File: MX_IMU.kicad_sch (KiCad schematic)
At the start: 31 parts, among them SW1 SW_SPST, U1 ld39150dt33-r, U200 STM32F405RGT6, U4 AT24C256, Y200 16MHz

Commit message: update
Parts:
- removed C4: 2u2, Capacitor_SMD:C_0603_1608Metric, symbol Device:C
- added C5: 2u2, Capacitor_SMD:C_0603_1608Metric, symbol Device:C_Small
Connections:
- net +3.3V: now also C5.1
- net GND: now also C5.2
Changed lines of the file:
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@@
 	(wire
 		(pts
-			(xy 203.2 35.56) (xy 203.2 34.29)
+			(xy 203.2 31.75) (xy 203.2 35.56)
 		)
 		(stroke
@@
 	(symbol
 		(lib_id "Device:C")
-		(at 203.2 30.48 0)
+		(at 177.8 30.48 0)
 		(unit 1)
 		(exclude_from_sim no)
@@
 		(on_board yes)
 		(dnp no)
-		(property "Reference" "C4"
-			(at 205.74 29.21 0)
+		(property "Reference" "C3"
+			(at 180.34 29.21 0)
 			(effects
 				(font
@@
 			)
 		)
-		(property "Value" "2u2"
-			(at 205.74 31.75 0)
+		(property "Value" "1u"
+			(at 180.34 31.75 0)
 			(effects
 				(font
@@
 		)
 		(property "Footprint" "Capacitor_SMD:C_0603_1608Metric"
-			(at 204.1652 34.29 0)
+			(at 178.7652 34.29 0)
 			(effects
 				(font
@@
 		)
 		(property "Datasheet" "~"
-			(at 203.2 30.48 0)
+			(at 177.8 30.48 0)
 			(effects
 				(font
@@
 		)
 		(property "Description" "Unpolarized capacitor"
-			(at 203.2 30.48 0)
+			(at 177.8 30.48 0)
 			(effects
 				(font
@@
 			(project "MX_IMU"
 				(path "/8ed38441-7d4e-4e89-870f-07e11c6dce38"
-					(reference "C4")
+					(reference "C3")
 					(unit 1)
 				)
@@
 	)
 	(symbol
-		(lib_id "Device:C")
-		(at 177.8 30.48 0)
+		(lib_id "Device:R_Small_US")
+		(at 241.3 80.01 0)
 		(unit 1)
 		(exclude_from_sim no)
@@
 		(on_board yes)
 		(dnp no)
-		(property "Reference" "C3"
-			(at 180.34 29.21 0)
+		(fields_autoplaced yes)
+		(property "Reference" "R14"
+			(at 243.078 78.7399 0)
 			(effects
 				(font
@@
 			)
 		)
-		(property "Value" "1u"
-			(at 180.34 31.75 0)
+		(property "Value" "330R"
+			(at 243.078 81.2799 0)
 			(effects
 				(font
@@
 			)
 		)
-		(property "Footprint" "Capacitor_SMD:C_0603_1608Metric"
-			(at 178.7652 34.29 0)
+		(property "Footprint" "Resistor_SMD:R_0402_1005Metric"
+			(at 241.3 80.01 0)
 			(effects
 				(font
@@
 		)
 		(property "Datasheet" "~"
-			(at 177.8 30.48 0)
+			(at 241.3 80.01 0)
 			(effects
 				(font
@@
 			)
 		)
-		(property "Description" "Unpolarized capacitor"
-			(at 177.8 30.48 0)
+		(property "Description" ""
+			(at 241.3 80.01 0)
 			(effects
 				(font
@@
 			(project "MX_IMU"
 				(path "/8ed38441-7d4e-4e89-870f-07e11c6dce38"
-					(reference "C3")
+					(reference "R14")
 					(unit 1)
 				)
@@
 	)
 	(symbol
-		(lib_id "Device:R_Small_US")
-		(at 241.3 80.01 0)
+		(lib_id "power:GND")
+		(at 241.3 96.52 0)
 		(unit 1)
 		(exclude_from_sim no)
@@
 		(dnp no)
 		(fields_autoplaced yes)
-		(property "Reference" "R14"
-			(at 243.078 78.7399 0)
+		(property "Reference" "#PWR038"
+			(at 241.3 102.87 0)
 			(effects
 				(font
 					(size 1.27 1.27)
 				)
-				(justify left)
+				(hide yes)
 			)
 		)
-		(property "Value" "330R"
-			(at 243.078 81.2799 0)
+		(property "Value" "GND"
+			(at 241.3 101.6 0)
 			(effects
 				(font
 					(size 1.27 1.27)
 				)
-				(justify left)
+				(hide yes)
 			)
 		)
-		(property "Footprint" "Resistor_SMD:R_0402_1005Metric"
-			(at 241.3 80.01 0)
+		(property "Footprint" ""
+			(at 241.3 96.52 0)
 			(effects
 				(font
@@
 			)
 		)
-		(property "Datasheet" "~"
-			(at 241.3 80.01 0)
+		(property "Datasheet" ""
+			(at 241.3 96.52 0)
 			(effects
 				(font
@@
 		)
 		(property "Description" ""
-			(at 241.3 80.01 0)
+			(at 241.3 96.52 0)
 			(effects
 				(font
 					(size 1.27 1.27)
 				)
-				(hide yes)
 			)
 		)
 		(pin "1"
 		)
-		(pin "2"
-		)
 		(instances
 			(project "MX_IMU"
 				(path "/8ed38441-7d4e-4e89-870f-07e11c6dce38"
-					(reference "R14")
+					(reference "#PWR038")
 					(unit 1)
 				)
@@
 	)
 	(symbol
-		(lib_id "power:GND")
-		(at 241.3 96.52 0)
+		(lib_id "Device:C_Small")
+		(at 203.2 29.21 0)
 		(unit 1)
 		(exclude_from_sim no)
@@
 		(on_board yes)
 		(dnp no)
-		(fields_autoplaced yes)
-		(property "Reference" "#PWR038"
-			(at 241.3 102.87 0)
+		(property "Reference" "C5"
+			(at 205.74 27.94 0)
 			(effects
 				(font
 					(size 1.27 1.27)
 				)
-				(hide yes)
+				(justify left)
 			)
 		)
-		(property "Value" "GND"
-			(at 241.3 101.6 0)
+		(property "Value" "2u2"
+			(at 205.74 30.48 0)
 			(effects
 				(font
 					(size 1.27 1.27)
 				)
-				(hide yes)
+				(justify left)
 			)
 		)
-		(property "Footprint" ""
-			(at 241.3 96.52 0)
+		(property "Footprint" "Capacitor_SMD:C_0603_1608Metric"
+			(at 203.2 29.21 0)
 			(effects
 				(font
@@
 			)
 		)
-		(property "Datasheet" ""
-			(at 241.3 96.52 0)
+		(property "Datasheet" "~"
+			(at 203.2 29.21 0)
 			(effects
 				(font
@@
 		)
 		(property "Description" ""
-			(at 241.3 96.52 0)
+			(at 203.2 29.21 0)
+			(effects
+				(font
+					(size 1.27 1.27)
+				)
+			)
+		)
+		(property "LCSC Part #" "C23630"
+			(at 203.2 29.21 0)
 			(effects
 				(font
 					(size 1.27 1.27)
 				)
+				(hide yes)
 			)
 		)
 		(pin "1"
 		)
+		(pin "2"
+		)
 		(instances
 			(project "MX_IMU"
 				(path "/8ed38441-7d4e-4e89-870f-07e11c6dce38"
-					(reference "#PWR038")
+					(reference "C5")
 					(unit 1)
 				)

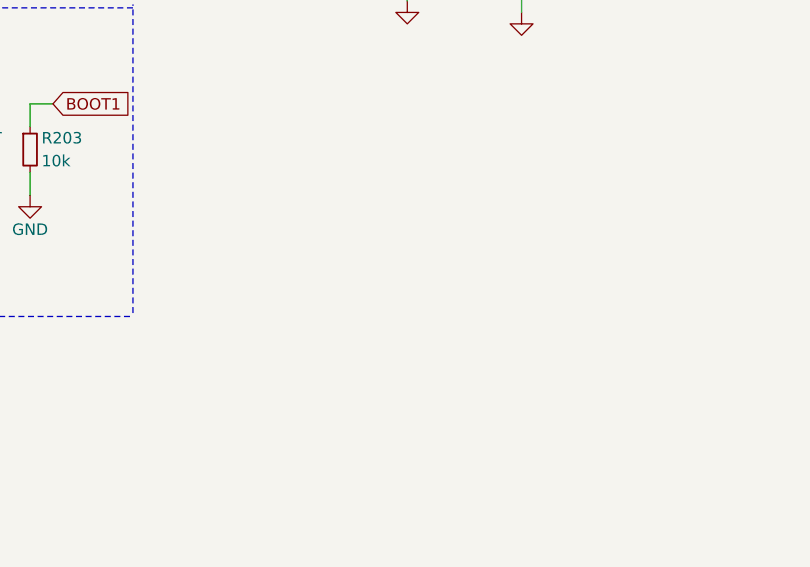
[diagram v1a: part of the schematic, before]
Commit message: add mountinghole in sch
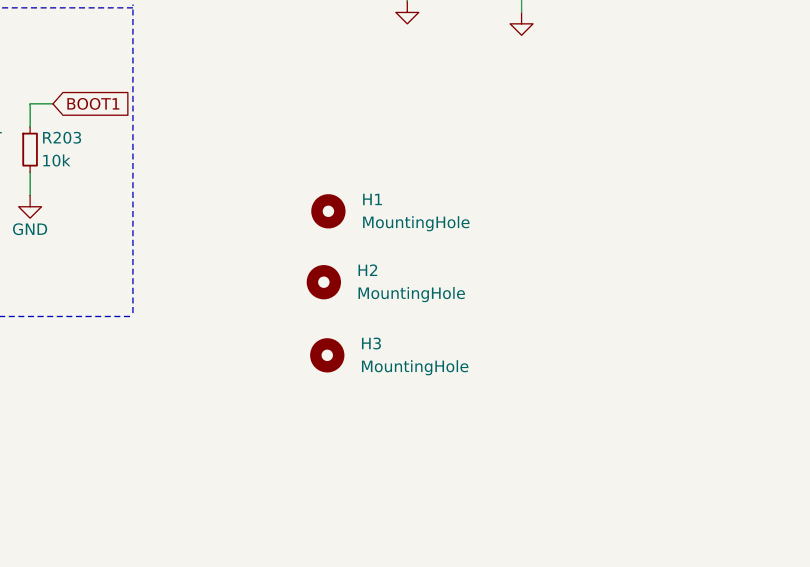
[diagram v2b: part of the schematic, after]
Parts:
- added H1, H2, H3: MountingHole, MountingHole:MountingHole_2mm, symbol Mechanical:MountingHole
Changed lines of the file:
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@@
+	)
+	(symbol
+		(lib_id "Mechanical:MountingHole")
+		(at 219.71 134.62 0)
+		(unit 1)
+		(exclude_from_sim no)
+		(in_bom no)
+		(on_board yes)
+		(dnp no)
+		(fields_autoplaced yes)
+		(property "Reference" "H3"
+			(at 223.393 133.3499 0)
+			(effects
+				(font
+					(size 1.27 1.27)
+				)
+				(justify left)
+			)
+		)
+		(property "Value" "MountingHole"
+			(at 223.393 135.8899 0)
+			(effects
+				(font
+					(size 1.27 1.27)
+				)
+				(justify left)
+			)
+		)
+		(property "Footprint" "MountingHole:MountingHole_2mm"
+			(at 219.71 134.62 0)
+			(effects
+				(font
+					(size 1.27 1.27)
+				)
+				(hide yes)
+			)
+		)
+		(property "Datasheet" "~"
+			(at 219.71 134.62 0)
+			(effects
+				(font
+					(size 1.27 1.27)
+				)
+				(hide yes)
+			)
+		)
+		(property "Description" "Mounting Hole without connection"
+			(at 219.71 134.62 0)
+			(effects
+				(font
+					(size 1.27 1.27)
+				)
+				(hide yes)
+			)
+		)
+		(instances
+			(project "MX_IMU"
+				(path "/8ed38441-7d4e-4e89-870f-07e11c6dce38"
+					(reference "H3")
+					(unit 1)
+				)
+			)
+		)
 	)
 	(symbol
@@
 	)
 	(symbol
+		(lib_id "Mechanical:MountingHole")
+		(at 219.329 126.492 0)
+		(unit 1)
+		(exclude_from_sim no)
+		(in_bom no)
+		(on_board yes)
+		(dnp no)
+		(fields_autoplaced yes)
+		(property "Reference" "H2"
+			(at 223.012 125.2219 0)
+			(effects
+				(font
+					(size 1.27 1.27)
+				)
+				(justify left)
+			)
+		)
+		(property "Value" "MountingHole"
+			(at 223.012 127.7619 0)
+			(effects
+				(font
+					(size 1.27 1.27)
+				)
+				(justify left)
+			)
+		)
+		(property "Footprint" "MountingHole:MountingHole_2mm"
+			(at 219.329 126.492 0)
+			(effects
+				(font
+					(size 1.27 1.27)
+				)
+				(hide yes)
+			)
+		)
+		(property "Datasheet" "~"
+			(at 219.329 126.492 0)
+			(effects
+				(font
+					(size 1.27 1.27)
+				)
+				(hide yes)
+			)
+		)
+		(property "Description" "Mounting Hole without connection"
+			(at 219.329 126.492 0)
+			(effects
+				(font
+					(size 1.27 1.27)
+				)
+				(hide yes)
+			)
+		)
+		(instances
+			(project "MX_IMU"
+				(path "/8ed38441-7d4e-4e89-870f-07e11c6dce38"
+					(reference "H2")
+					(unit 1)
+				)
+			)
+		)
+	)
+	(symbol
 		(lib_id "power:+3.3V")
 		(at 162.56 142.24 0)
@@
 					(unit 1)
 				)
+			)
+		)
+	)
+	(symbol
+		(lib_id "Mechanical:MountingHole")
+		(at 219.837 118.618 0)
+		(unit 1)
+		(exclude_from_sim no)
+		(in_bom no)
+		(on_board yes)
+		(dnp no)
+		(fields_autoplaced yes)
+		(property "Reference" "H1"
+			(at 223.52 117.3479 0)
+			(effects
+				(font
+					(size 1.27 1.27)
+				)
+				(justify left)
+			)
+		)
+		(property "Value" "MountingHole"
+			(at 223.52 119.8879 0)
+			(effects
+				(font
+					(size 1.27 1.27)
+				)
+				(justify left)
+			)
+		)
+		(property "Footprint" "MountingHole:MountingHole_2mm"
+			(at 219.837 118.618 0)
+			(effects
+				(font
+					(size 1.27 1.27)
+				)
+				(hide yes)
+			)
+		)
+		(property "Datasheet" "~"
+			(at 219.837 118.618 0)
+			(effects
+				(font
+					(size 1.27 1.27)
+				)
+				(hide yes)
+			)
+		)
+		(property "Description" "Mounting Hole without connection"
+			(at 219.837 118.618 0)
+			(effects
+				(font
+					(size 1.27 1.27)
+				)
+				(hide yes)
+			)
+		)
+		(instances
+			(project ""
+				(path "/8ed38441-7d4e-4e89-870f-07e11c6dce38"
+					(reference "H1")
+					(unit 1)
+				)
